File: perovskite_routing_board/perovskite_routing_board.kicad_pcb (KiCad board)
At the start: 2 copper layers, 57 x 52.2 mm, 7 parts, among them J1 Conn_01x08, J2 Conn_01x08, J3 Conn_01x08, J4 Conn_01x08, J5 Conn_01x08, J6 Conn_01x08, J7 G125-MH12605M4R

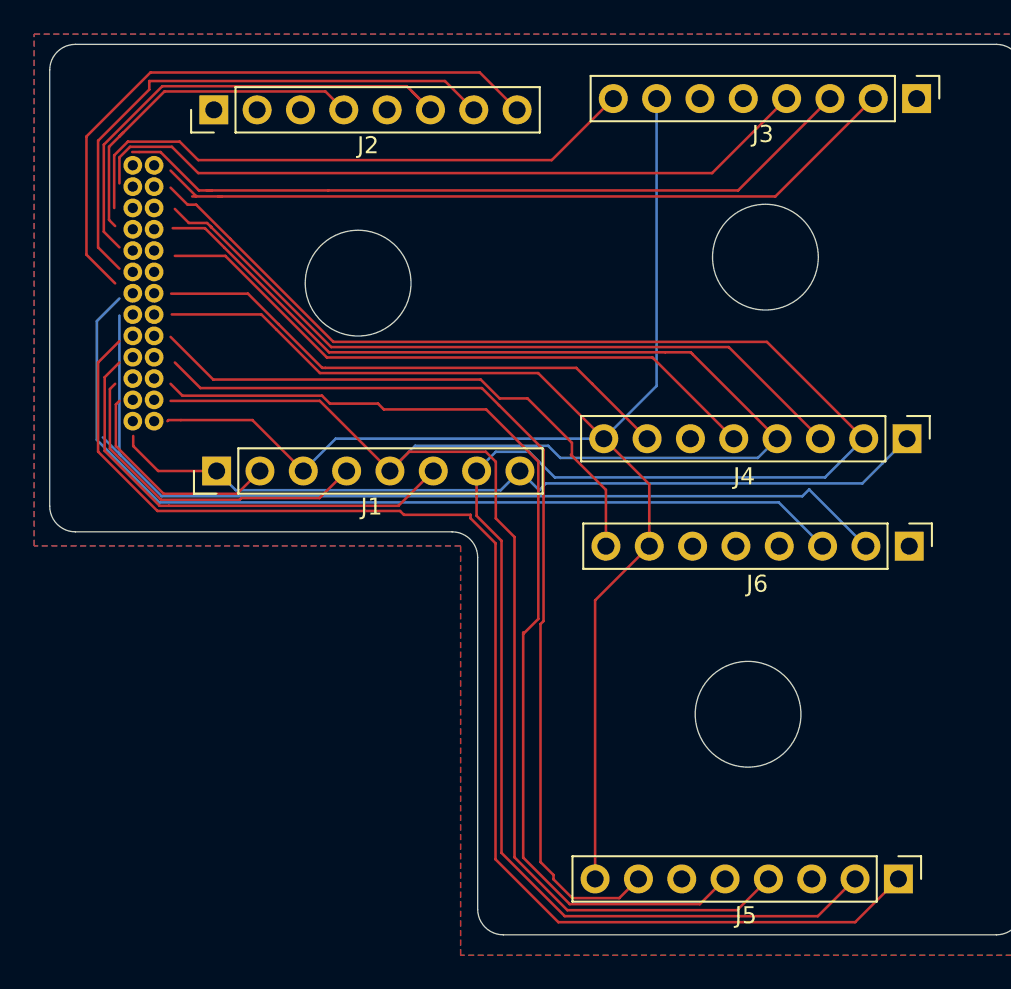
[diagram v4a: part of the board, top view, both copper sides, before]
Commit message: routing board done and nice and pretty
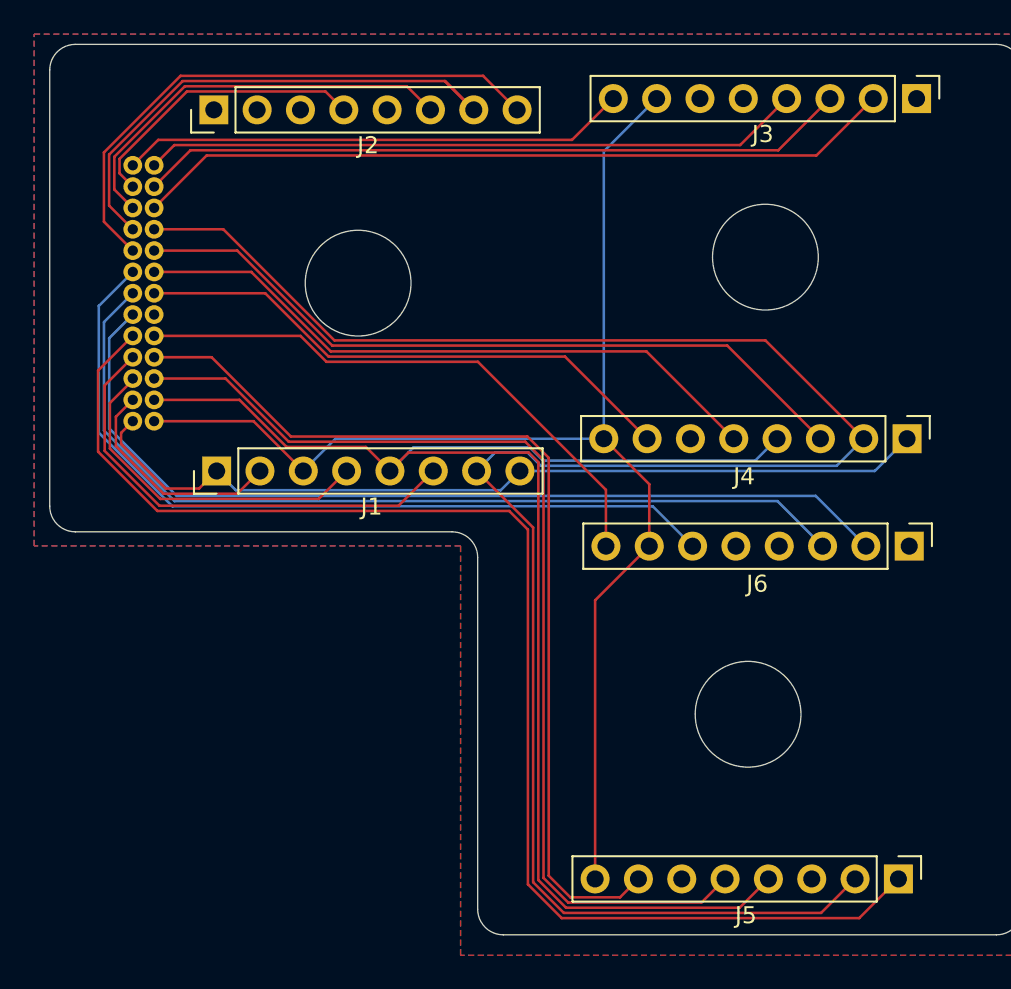
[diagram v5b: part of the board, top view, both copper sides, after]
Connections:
- J2 pad 4: CELL3 -> CELL_3
- J7 pad 1: Net-(J7-Pad1) -> CP
- J7 pad 10: Net-(J7-Pad10) -> ALERT1
- J7 pad 11: Net-(J7-Pad11) -> CELL_2
- J7 pad 12: Net-(J7-Pad12) -> CELL_3
- J7 pad 13: Net-(J7-Pad13) -> CELL_7
- J7 pad 14: Net-(J7-Pad14) -> VDD
- J7 pad 15: Net-(J7-Pad15) -> SDA
- J7 pad 16: Net-(J7-Pad16) -> CELL_17
- J7 pad 17: Net-(J7-Pad17) -> CELL_18
- J7 pad 18: Net-(J7-Pad18) -> CELL_13
- J7 pad 19: Net-(J7-Pad19) -> GND
- J7 pad 2: Net-(J7-Pad2) -> CELL_6
- J7 pad 20: Net-(J7-Pad20) -> CELL_12
- J7 pad 21: Net-(J7-Pad21) -> CELL_11
- J7 pad 22: Net-(J7-Pad22) -> CELL_10
- J7 pad 23: Net-(J7-Pad23) -> SCL
- J7 pad 24: Net-(J7-Pad24) -> CELL_9
- J7 pad 25: Net-(J7-Pad25) -> ALERT2
- J7 pad 26: Net-(J7-Pad26) -> CELL_8
- J7 pad 3: Net-(J7-Pad3) -> CELL_5
- J7 pad 4: Net-(J7-Pad4) -> CELL_4
- J7 pad 5: Net-(J7-Pad5) -> CELL_16
- J7 pad 6: Net-(J7-Pad6) -> CELL_15
- J7 pad 7: Net-(J7-Pad7) -> ALERT3
- J7 pad 8: Net-(J7-Pad8) -> CELL_14
- J7 pad 9: Net-(J7-Pad9) -> CELL_1
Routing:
- net CELL_14: track 0.00 -> 47.8 mm
- net SDA: track 126.7 -> 88.4 mm
- net VDD: track 105.4 -> 77.8 mm
- net CELL3: track 20.7 -> 0.00 mm
- net CELL_3: track 0.00 -> 17.2 mm
- net CELL_7: track 34.6 -> 29.8 mm
- net CELL_2: track 29.1 -> 24.3 mm
- net CELL_8: track 43.3 -> 38.7 mm
- net CELL_1: track 37.0 -> 33.4 mm
- net ALERT2: track 44.4 -> 41.8 mm
- net CP: track 49.8 -> 51.5 mm
- net CELL_16: track 77.4 -> 79.0 mm
- net CELL_15: track 55.9 -> 54.5 mm
- net ALERT1: track 32.5 -> 31.2 mm
- net CELL_18: track 55.2 -> 56.3 mm
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
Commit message: added pull up resistor
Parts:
- added R1: R, Resistor_SMD:R_0603_1608Metric, F.Cu at (130.6, 95.2)
- added R2: R, Resistor_SMD:R_0603_1608Metric, F.Cu at (130.6, 96.8)
- moved J1 50.1 mm to (124.3, 100.9)
- moved J3 50.1 mm to (165.3, 79.1)
- moved J2 50.1 mm to (124.1, 79.7)
- moved J4 50.1 mm to (164.7, 99.0)
- moved J5 50.1 mm to (164.2, 124.8)
- moved J7 50.1 mm to (119.4, 98.0)
- moved J6 50.1 mm to (164.9, 105.3)
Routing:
- net VDD: track 77.8 -> 91.7 mm, vias 0 -> 1
- net SCL: track 116.7 -> 129.9 mm, vias 0 -> 1
- net SDA: track 88.4 -> 97.6 mm, vias 0 -> 1

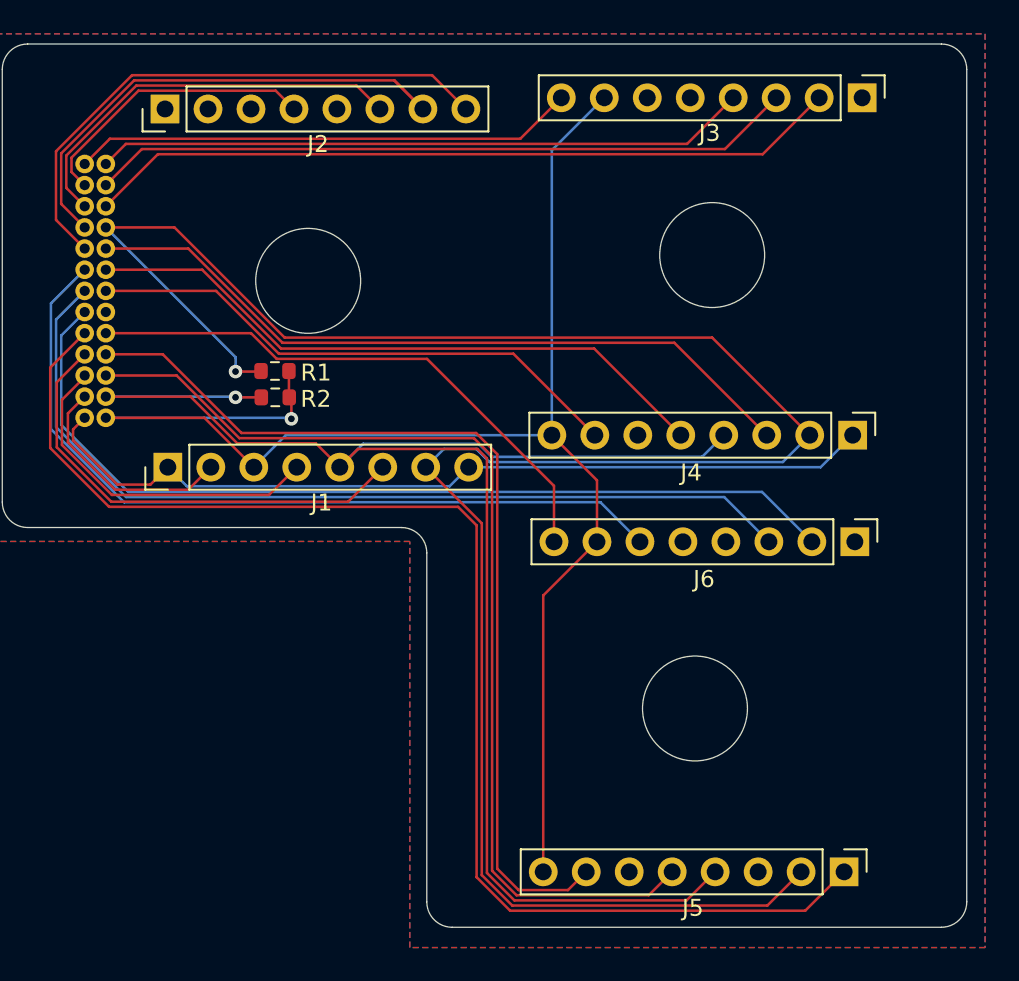
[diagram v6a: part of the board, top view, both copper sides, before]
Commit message: Updating designs
- Generate gerbers
- Generate renders
- Working on layout for payload controller
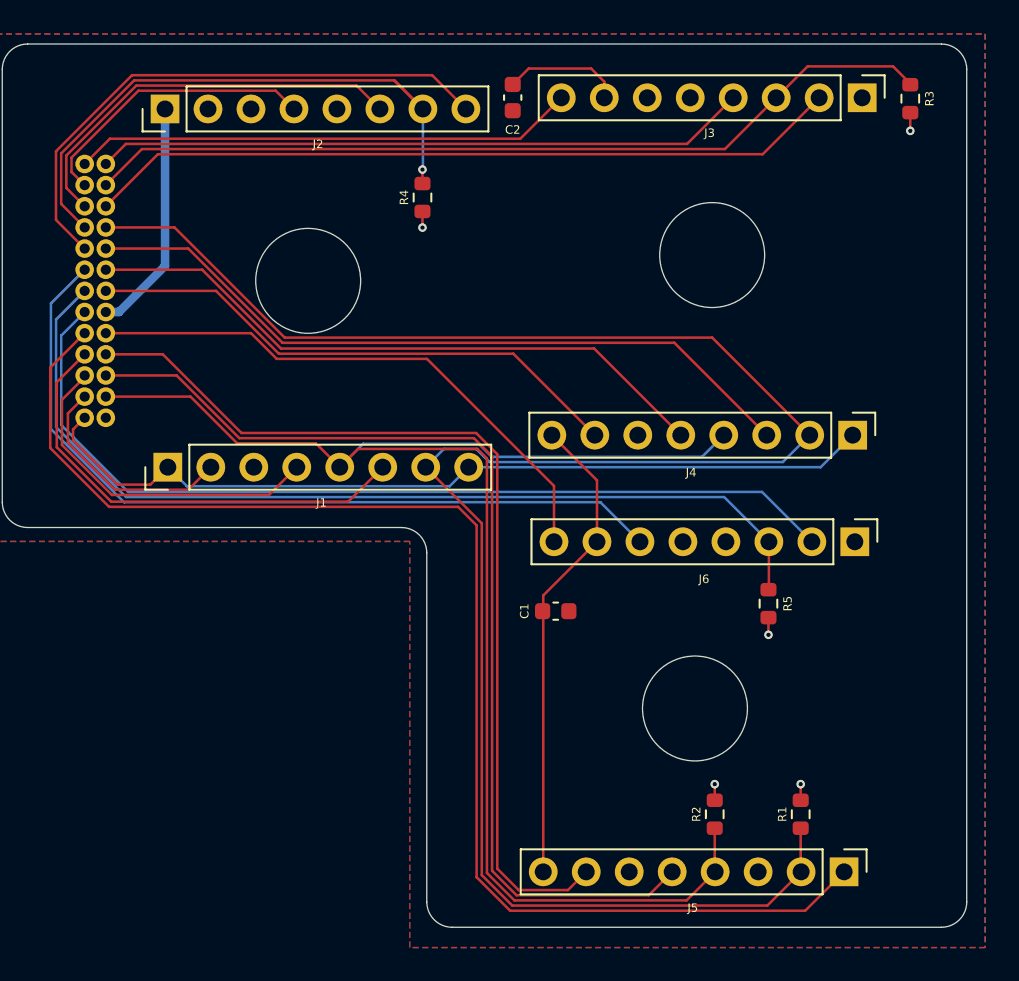
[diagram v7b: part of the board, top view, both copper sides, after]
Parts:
- added C1: 0.1u, Capacitor_SMD:C_0603_1608Metric, F.Cu at (147.2, 109.4)
- added C2: 0.1u, Capacitor_SMD:C_0603_1608Metric, F.Cu at (144.7, 79.1)
- added R3: R, Resistor_SMD:R_0603_1608Metric, F.Cu at (168.1, 79.1)
- added R4: R, Resistor_SMD:R_0603_1608Metric, F.Cu at (139.3, 85.0)
- added R5: R, Resistor_SMD:R_0603_1608Metric, F.Cu at (159.8, 109.0)
- moved R1 40.6 mm to (161.7, 121.4), turned to 270 degrees
- moved R2 35.8 mm to (156.6, 121.4), turned to 270 degrees
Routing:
- net VDD: track 91.7 -> 40.3 mm, vias 1 -> 5
- net GND: track 0.79 -> 14.7 mm
- net SCL: track 129.9 -> 119.3 mm, vias 1 -> 0
- net ALERT2: track 41.8 -> 50.9 mm
- net SDA: track 97.6 -> 91.0 mm, vias 1 -> 0
- net ALERT1: track 31.2 -> 35.6 mm, vias 0 -> 1
- net ALERT3: track 53.7 -> 56.5 mm
- added copper zone on B.Cu, net VDD
- removed copper zone on B.Cu, net GND
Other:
- rule pad_to_mask_clearance: 0.0508 -> 0
